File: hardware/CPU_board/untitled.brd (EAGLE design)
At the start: 128.9 x 94.9 mm, 51 parts, among them IC1 MAX232ECWE, IC2 MAX232ECWE, IC3 AM29F040J, IC4 74HCT138D, IC5 LM2596S, J2 POWER_JACKSLT, U1 AS6C4008-55SIN, Y1 CRYSTAL-GROUNDEDSMD-5X3.2

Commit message: PCB update (work in progress)
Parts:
- moved R8 33.4 mm to (116.6, 53.7), turned to 180 degrees
- moved R1 25.5 mm to (110.5, 58.1), turned to 180 degrees
- moved R12 15.8 mm to (90.3, 60.7)
- moved R7 11.5 mm to (90.3, 62.2)
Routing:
- net 5V: track 146.2 -> 168.1 mm
- net D3: track 147.4 -> 138.2 mm
- net N$27: track 14.8 -> 23.3 mm
- net D2: track 153.6 -> 159.0 mm
- net D4: track 140.7 -> 135.5 mm
- net D5: track 139.7 -> 135.9 mm
- net N$29: track 0.00 -> 3.79 mm
- net N$30: track 14.8 -> 11.5 mm
- net D6: track 132.1 -> 129.9 mm
- net N$33: track 19.5 -> 17.8 mm
- net N$34: track 27.1 -> 25.4 mm
- net D1: track 160.0 -> 158.8 mm
- net CF_CS0: track 57.0 -> 58.2 mm
- net A0: track 186.7 -> 185.9 mm
- net D0: track 148.1 -> 147.3 mm

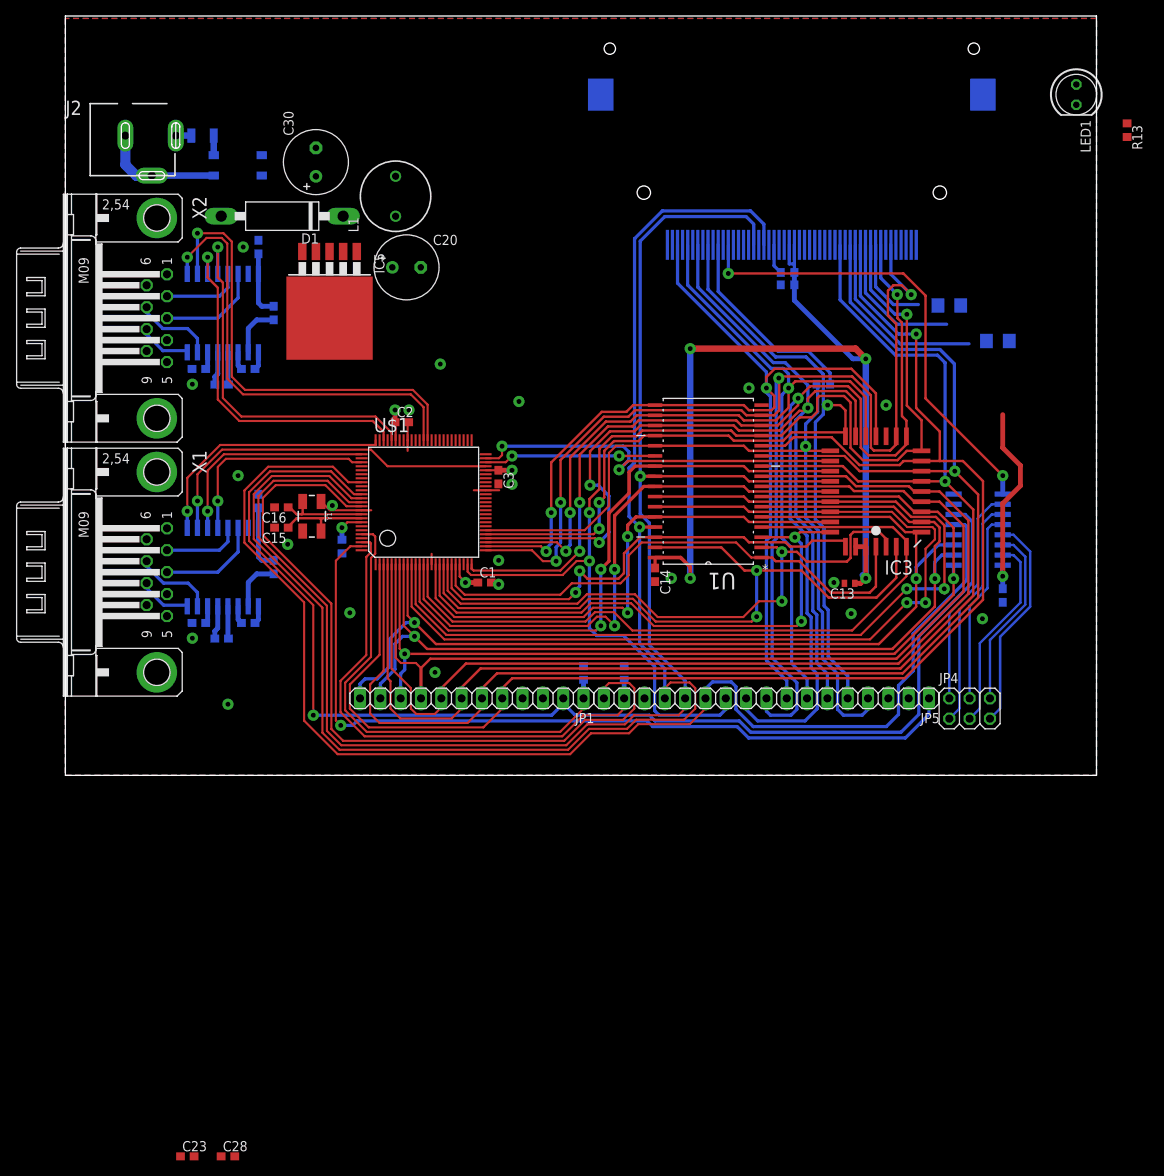
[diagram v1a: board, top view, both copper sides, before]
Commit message: PCB design updated. NMI, WAIT, BUSREQ and BUSACK signals routed to additional connector
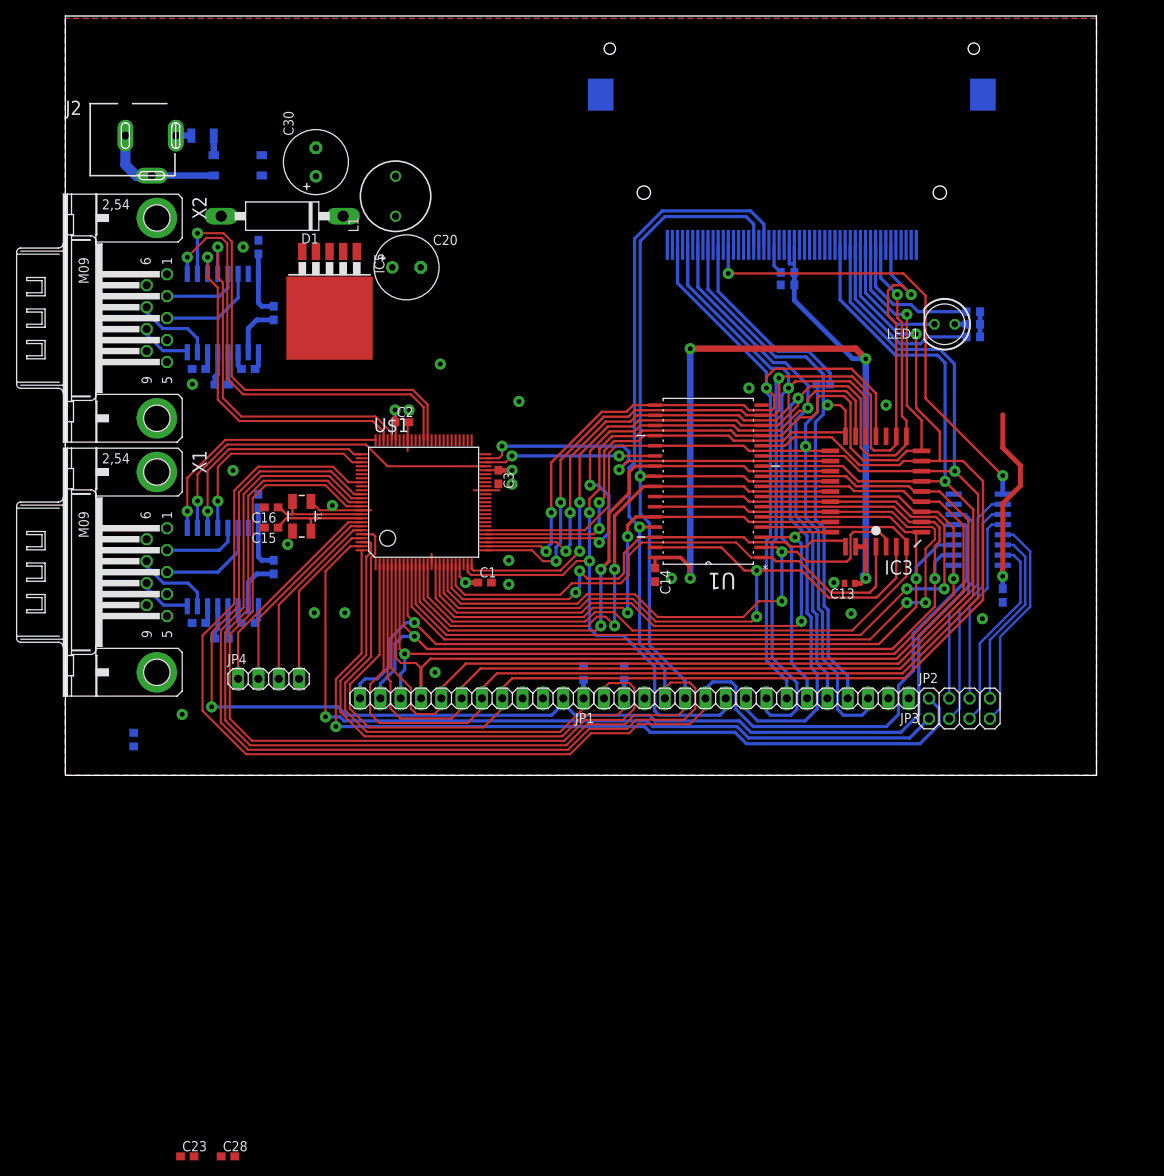
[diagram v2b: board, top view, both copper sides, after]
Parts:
- removed JP5: (no value), pinhead:1X17
- added JP2: (no value), pinhead:2X04
- added JP3: (no value), pinhead:1X16
- JP4: device pinhead:2X03 -> pinhead:1X04
- R1, R8: device rcl:R1206 -> rcl:R0603
- moved JP4 87.7 mm to (25.4, 11.4)
- moved R3 35.5 mm to (8.53, 3.84)
- moved LED1 33.1 mm to (109.9, 55.8), turned to 180 degrees
- moved R13 31.0 mm to (113.5, 55.8), flipped to the bottom, turned to 180 degrees
- moved R8 3.12 mm to (113.5, 54.2)
- moved R1 3.10 mm to (113.5, 57.3)
- moved C15 1.27 mm to (25.7, 30.3)
- moved C16 1.27 mm to (25.7, 32.9)
- moved Y1 1.27 mm to (29.5, 31.8)
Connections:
- new net !BUSACK: JP4.2, U$1.94
- new net !BUSREQ: JP4.3, U$1.95
- net !INT: now also JP3.15; no longer JP5.16
- net !IORQ: now also JP3.11; no longer JP5.12
- net !IRQ1: now also JP2.1; no longer JP5.1
- net !IRQ2: now also JP2.2
- net !MRQ_NOT_CONNECTED: now also JP3.14; no longer JP5.15
- net !NMI: now also JP4.4
- net !RD: now also JP3.12; no longer JP5.13
- net !WAIT: now also JP4.1
- net !WR: now also JP3.13; no longer JP5.14
- net CLK: now also JP3.16; no longer JP5.17
- net CS0: now also JP2.5; no longer JP4.3
- net CS1: now also JP2.8; no longer JP4.6
- net CS2: now also JP2.7; no longer JP4.5
- net CS3: now also JP2.6; no longer JP4.4
- net CS4: now also JP2.3; no longer JP4.1
- net CS5: now also JP2.4; no longer JP4.2
- net D0: now also JP3.10; no longer JP5.11
- net D1: now also JP3.9; no longer JP5.10
- net D2: now also JP3.8; no longer JP5.9
- net D3: now also JP3.7; no longer JP5.8
- net D4: now also JP3.6; no longer JP5.7
- net D5: now also JP3.5; no longer JP5.6
- net D6: now also JP3.4; no longer JP5.5
- net D7: now also JP3.3; no longer JP5.4
- net RX: now also JP3.1; no longer JP5.2
- net TX: now also JP3.2; no longer JP5.3
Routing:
- net !IRQ2: track 0.00 -> 104.5 mm, vias 0 -> 1
- net !BUSACK: track 0.00 -> 25.2 mm
- net !BUSREQ: track 0.00 -> 23.5 mm
- net !WAIT: track 4.25 -> 26.9 mm, vias 1 -> 0
- net !NMI: track 0.00 -> 21.5 mm
- net !IORQ: track 163.1 -> 174.9 mm
- net !M1: track 156.6 -> 168.0 mm
- net !RD: track 198.4 -> 209.2 mm
- net !WR: track 189.2 -> 200.0 mm
- net CLK: track 94.8 -> 105.7 mm
- net N$30: track 11.5 -> 17.9 mm
- net 5V: track 168.1 -> 171.3 mm
- net N$33: track 17.8 -> 16.2 mm
- net N$32: track 0.00 -> 1.46 mm
- net OSC_OUT: track 11.4 -> 12.6 mm
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
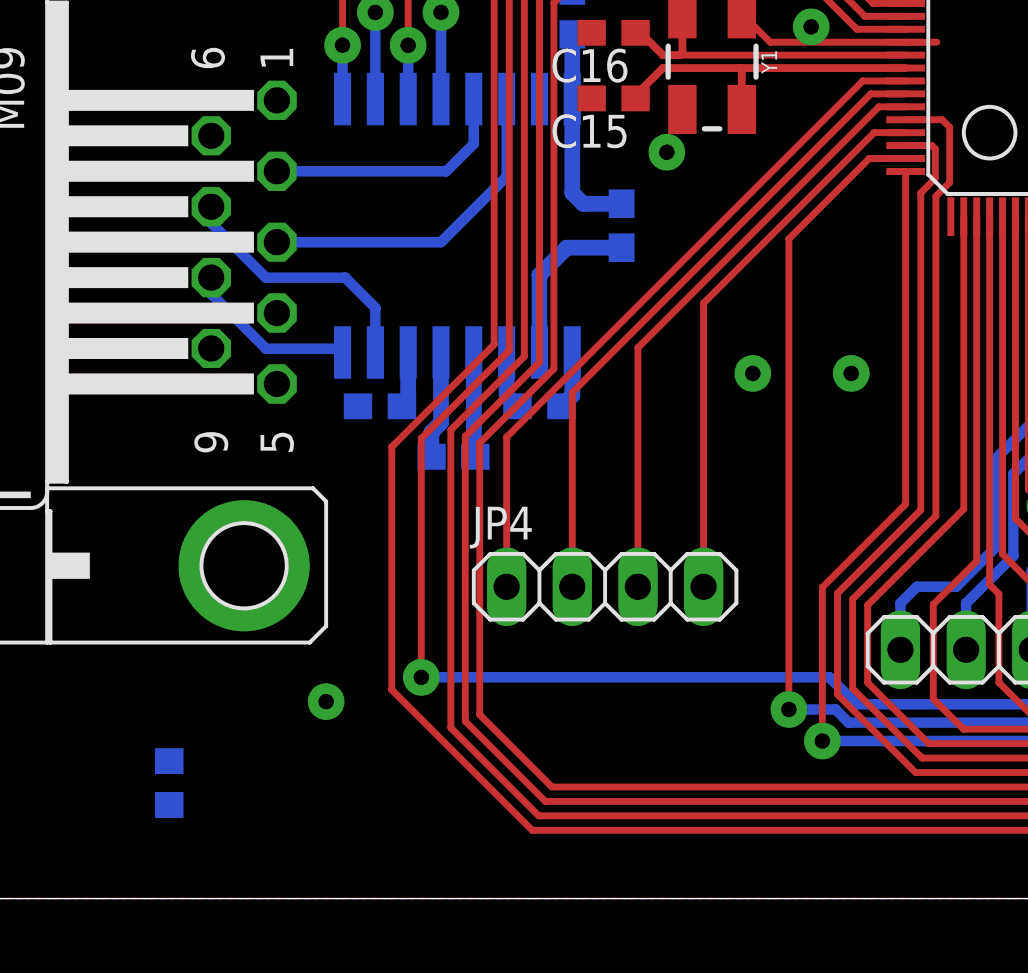
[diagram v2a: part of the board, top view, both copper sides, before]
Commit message: Resistor network added
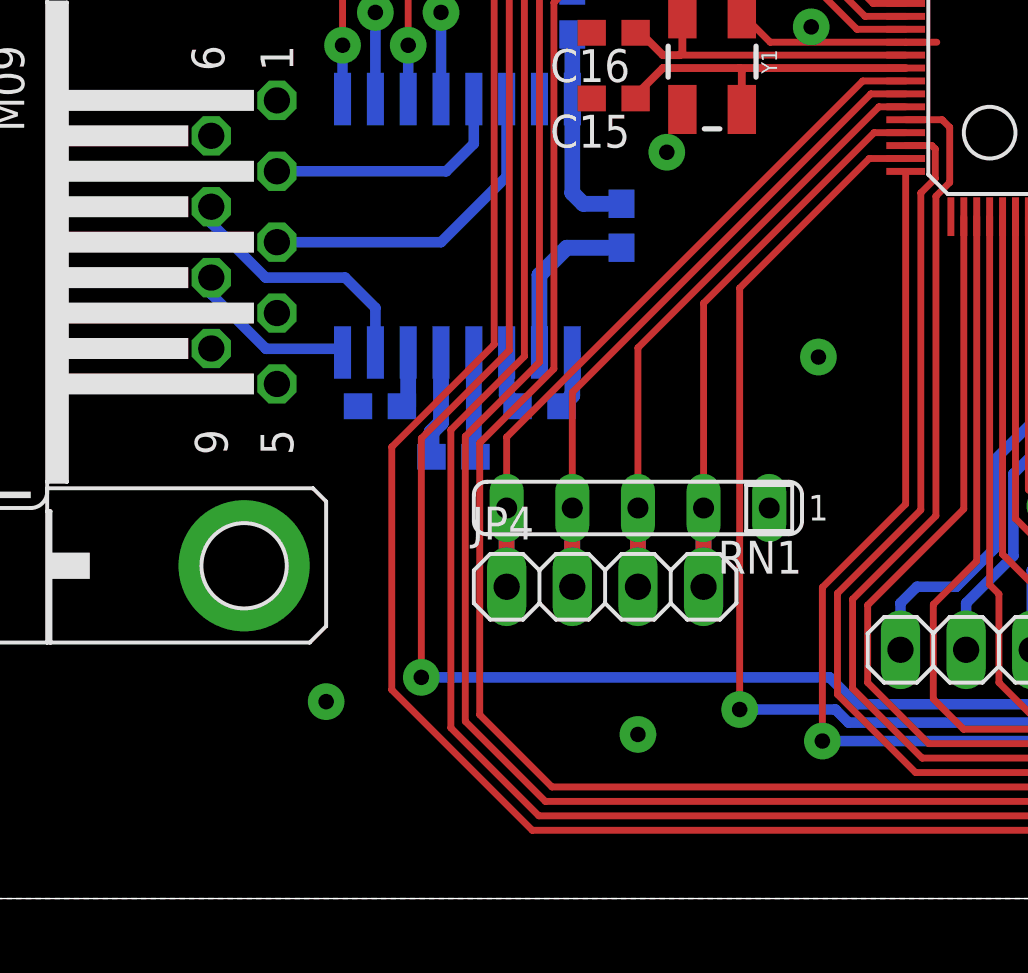
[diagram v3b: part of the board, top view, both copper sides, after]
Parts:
- removed R3: (no value), rcl:R0603
- added RN1: (no value), resistor-sil:SIL5
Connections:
- net !BUSACK: now also RN1.4
- net !BUSREQ: now also RN1.3
- net !NMI: now also RN1.2
- net !WAIT: now also RN1.5; no longer R3.1
- net 5V: now also RN1.1; no longer R3.2
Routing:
- net !WAIT: track 26.9 -> 30.0 mm
- net !BUSREQ: track 23.5 -> 26.5 mm
- net !BUSACK: track 25.2 -> 28.3 mm
- net !NMI: track 21.5 -> 24.6 mm
- net !IRQ1: track 101.6 -> 104.2 mm
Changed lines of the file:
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@@
 <element name="IC4" library="74xx-eu" package="SO16" value="74HCT138D" x="114.0968" y="30.0736" rot="MR90"/>
 <element name="C17" library="rcl" package="C0603" value="" x="117.1702" y="21.844" rot="MR270"/>
-<element name="R3" library="rcl" package="R0603" value="" x="8.5344" y="3.8354" rot="MR270"/>
 <element name="R4" library="rcl" package="R0603" value="" x="69.85" y="12.1666" rot="MR90"/>
 <element name="R5" library="rcl" package="R0603" value="" x="64.77" y="12.1666" rot="MR90"/>
@@
 <element name="JP3" library="pinhead" package="1X16" value="" x="86.36" y="8.9916" rot="R180"/>
 <element name="JP4" library="pinhead" package="1X04" value="" x="25.4" y="11.43"/>
+<element name="RN1" library="resistor-sil" package="SIL5" value="" x="26.67" y="14.478" rot="R180">
+<attribute name="OC_NEWARK" value="unknown" x="26.67" y="14.478" size="1.778" layer="27" rot="R180" display="off"/>
+<attribute name="MPN" value="" x="26.67" y="14.478" size="1.778" layer="27" rot="R180" display="off"/>
+<attribute name="MF" value="" x="26.67" y="14.478" size="1.778" layer="27" rot="R180" display="off"/>
+<attribute name="OC_FARNELL" value="unknown" x="26.67" y="14.478" size="1.778" layer="27" rot="R180" display="off"/>
+</element>
 </elements>
 <signals>
@@
 <via x="14.605" y="6.985" extent="1-16" drill="0.6" diameter="1.4224" shape="octagon"/>
 <contactref element="JP1" pad="4"/>
-<via x="34.925" y="19.685" extent="1-16" drill="0.6" diameter="1.4224" shape="octagon"/>
+<via x="33.655" y="20.32" extent="1-16" drill="0.6" diameter="1.4224" shape="octagon"/>
 <via x="27.7876" y="28.2448" extent="1-16" drill="0.6" diameter="1.4224" shape="octagon"/>
 <via x="55.4228" y="23.241" extent="1-16" drill="0.6" diameter="1.4224" shape="octagon"/>
@@
 <contactref element="C17" pad="2"/>
 <via x="114.6302" y="18.9484" extent="1-16" drill="0.6" diameter="1.4224" shape="octagon"/>
-<via x="31.115" y="19.685" extent="1-16" drill="0.6" diameter="1.4224" shape="octagon"/>
+<via x="26.67" y="5.715" extent="1-16" drill="0.6" diameter="1.4224" shape="octagon"/>
 <wire x1="94.2975" y1="65.675" x2="95.5675" y2="65.675" width="0" layer="19" extent="16-16"/>
 <wire x1="93.0275" y1="65.675" x2="94.2975" y2="65.675" width="0" layer="19" extent="16-16"/>
@@
 <wire x1="85.4075" y1="65.675" x2="86.6775" y2="65.675" width="0" layer="19" extent="16-16"/>
 <wire x1="84.1375" y1="65.675" x2="85.4075" y2="65.675" width="0" layer="19" extent="16-16"/>
-<wire x1="16.09" y1="-48.26" x2="14.605" y2="6.985" width="0" layer="19" extent="1-1"/>
-<wire x1="21.17" y1="-48.26" x2="16.09" y2="-48.26" width="0" layer="19" extent="1-1"/>
+<wire x1="21.17" y1="-48.26" x2="26.67" y2="5.715" width="0" layer="19" extent="1-1"/>
+<wire x1="16.09" y1="-48.26" x2="21.17" y2="-48.26" width="0" layer="19" extent="1-1"/>
 </signal>
 <signal name="5V">
@@
 <wire x1="119.38" y1="35.56" x2="119.38" y2="38.1" width="0.6096" layer="1"/>
 <wire x1="117.1702" y1="40.3098" x2="119.38" y2="38.1" width="0.6096" layer="1"/>
-<contactref element="R3" pad="2"/>
 <contactref element="R4" pad="2"/>
 <contactref element="R5" pad="2"/>
@@
 <wire x1="114.3372" y1="54.1782" x2="114.3372" y2="55.753" width="0.6096" layer="16"/>
 <wire x1="114.3372" y1="55.753" x2="114.3372" y2="57.3278" width="0.6096" layer="16"/>
+<contactref element="RN1" pad="1"/>
 <wire x1="117.1702" y1="44.45" x2="114.3372" y2="54.1782" width="0" layer="19" extent="1-16"/>
 <wire x1="100.0506" y1="51.435" x2="114.3372" y2="54.1782" width="0" layer="19" extent="16-16"/>
@@
 <wire x1="41.2802" y1="41.2526" x2="52.5302" y2="37.5026" width="0" layer="19" extent="1-1"/>
 <wire x1="24.13" y1="32.805" x2="41.2802" y2="41.2526" width="0" layer="19" extent="1-16"/>
+<wire x1="31.75" y1="14.478" x2="26.035" y2="26.25" width="0" layer="19" extent="16-16"/>
 <wire x1="26.035" y1="58" x2="41.2124" y2="45.0342" width="0" layer="19" extent="16-16"/>
 <wire x1="31.3182" y1="64.8462" x2="24.13" y2="64.555" width="0" layer="19" extent="1-16"/>
 <wire x1="31.3182" y1="74.2442" x2="31.3182" y2="64.8462" width="0" layer="19" extent="1-1"/>
 <wire x1="41.275" y1="74.255" x2="31.3182" y2="74.2442" width="0" layer="19" extent="1-1"/>
-<wire x1="8.5344" y1="2.9854" x2="24.55" y2="26.25" width="0" layer="19" extent="16-16"/>
-<wire x1="19.47" y1="-48.26" x2="8.5344" y2="2.9854" width="0" layer="19" extent="1-16"/>
+<wire x1="19.47" y1="-48.26" x2="31.75" y2="14.478" width="0" layer="19" extent="1-1"/>
 </signal>
 <signal name="N$7">
@@
 <contactref element="U$1" pad="99"/>
 <wire x1="37.0302" y1="28.0026" x2="35.6226" y2="28.0026" width="0.2667" layer="1"/>
-<wire x1="35.6226" y1="28.0026" x2="32.512" y2="24.892" width="0.2667" layer="1"/>
-<via x="32.512" y="6.6802" extent="1-16" drill="0.6" diameter="1.4224" shape="octagon"/>
+<wire x1="35.6226" y1="28.0026" x2="30.607" y2="22.987" width="0.2667" layer="1"/>
+<via x="30.607" y="6.6802" extent="1-16" drill="0.6" diameter="1.4224" shape="octagon"/>
 <wire x1="34.8234" y1="6.1722" x2="72.7202" y2="6.1722" width="0.4064" layer="16"/>
 <wire x1="72.7202" y1="6.1722" x2="73.4314" y2="5.461" width="0.4064" layer="16"/>
@@
 <contactref element="JP2" pad="1"/>
 <wire x1="105.537" y1="4.0386" x2="107.95" y2="6.4516" width="0.4064" layer="16"/>
-<wire x1="32.512" y1="6.6802" x2="32.512" y2="24.892" width="0.2667" layer="1"/>
-<wire x1="32.512" y1="6.6802" x2="34.3154" y2="6.6802" width="0.4064" layer="16"/>
+<wire x1="30.607" y1="6.6802" x2="30.607" y2="22.987" width="0.2667" layer="1"/>
+<wire x1="30.607" y1="6.6802" x2="34.3154" y2="6.6802" width="0.4064" layer="16"/>
 <wire x1="34.3154" y1="6.6802" x2="34.8234" y2="6.1722" width="0.4064" layer="16"/>
 </signal>
@@
 <wire x1="37.0302" y1="29.0026" x2="35.8098" y2="29.0026" width="0.2667" layer="1"/>
 <wire x1="35.8098" y1="29.0026" x2="29.21" y2="22.4028" width="0.2667" layer="1"/>
-<wire x1="29.21" y1="22.4028" x2="29.21" y2="11.43" width="0.2667" layer="1"/>
+<contactref element="RN1" pad="2"/>
+<wire x1="29.21" y1="11.43" x2="29.21" y2="14.478" width="0.6096" layer="16"/>
+<wire x1="29.21" y1="11.43" x2="29.21" y2="14.478" width="0.6096" layer="1"/>
+<wire x1="29.21" y1="22.4028" x2="29.21" y2="14.478" width="0.2667" layer="1"/>
 </signal>
 <signal name="!WAIT">
 <contactref element="U$1" pad="93"/>
-<contactref element="R3" pad="1"/>
 <contactref element="JP4" pad="1"/>
 <wire x1="37.0302" y1="31.0026" x2="35.3714" y2="31.0026" width="0.2667" layer="1"/>
 <wire x1="35.3714" y1="31.0026" x2="21.59" y2="17.2212" width="0.2667" layer="1"/>
-<wire x1="21.59" y1="17.2212" x2="21.59" y2="11.43" width="0.2667" layer="1"/>
-<wire x1="8.5344" y1="4.6854" x2="21.59" y2="11.43" width="0" layer="19" extent="16-16"/>
+<contactref element="RN1" pad="5"/>
+<wire x1="21.59" y1="11.43" x2="21.59" y2="14.478" width="0.6096" layer="16"/>
+<wire x1="21.59" y1="11.43" x2="21.59" y2="14.478" width="0.6096" layer="1"/>
+<wire x1="21.59" y1="17.2212" x2="21.59" y2="14.478" width="0.2667" layer="1"/>
 </signal>
 <signal name="!HLT">
@@
 <wire x1="37.0302" y1="30.5026" x2="35.6842" y2="30.5026" width="0.2667" layer="1"/>
 <wire x1="35.6842" y1="30.5026" x2="24.13" y2="18.9484" width="0.2667" layer="1"/>
-<wire x1="24.13" y1="18.9484" x2="24.13" y2="11.43" width="0.2667" layer="1"/>
+<contactref element="RN1" pad="4"/>
+<wire x1="24.13" y1="11.43" x2="24.13" y2="14.478" width="0.6096" layer="16"/>
+<wire x1="24.13" y1="11.43" x2="24.13" y2="14.478" width="0.6096" layer="1"/>
+<wire x1="24.13" y1="18.9484" x2="24.13" y2="14.478" width="0.2667" layer="1"/>
 </signal>
 <signal name="!BUSREQ">
@@
 <wire x1="37.0302" y1="30.0026" x2="35.997" y2="30.0026" width="0.2667" layer="1"/>
 <wire x1="35.997" y1="30.0026" x2="26.67" y2="20.6756" width="0.2667" layer="1"/>
-<wire x1="26.67" y1="20.6756" x2="26.67" y2="11.43" width="0.2667" layer="1"/>
+<contactref element="RN1" pad="3"/>
+<wire x1="26.67" y1="11.43" x2="26.67" y2="14.478" width="0.6096" layer="16"/>
+<wire x1="26.67" y1="11.43" x2="26.67" y2="14.478" width="0.6096" layer="1"/>
+<wire x1="26.67" y1="20.6756" x2="26.67" y2="14.478" width="0.2667" layer="1"/>
 </signal>
 </signals>
